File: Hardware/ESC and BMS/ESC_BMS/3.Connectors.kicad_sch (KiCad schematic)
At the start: 11 parts, among them J401 1mm2_connector, J402 1mm2_connector, J403 1mm2_connector, J404 JST_8PH_2mm, J405 JST_3PH_2mm, J406 1mm2_connector, J407 1mm2_connector, J408 1mm2_connector, J409 1mm2_connector, J410 DC power jack, J411 DC power jack GND

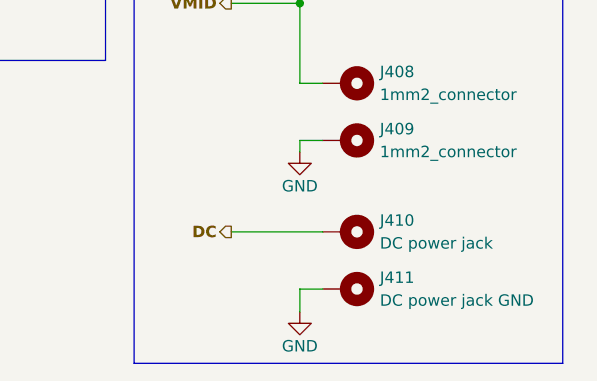
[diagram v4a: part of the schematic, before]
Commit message: ESC/BMS fully ready for PCB
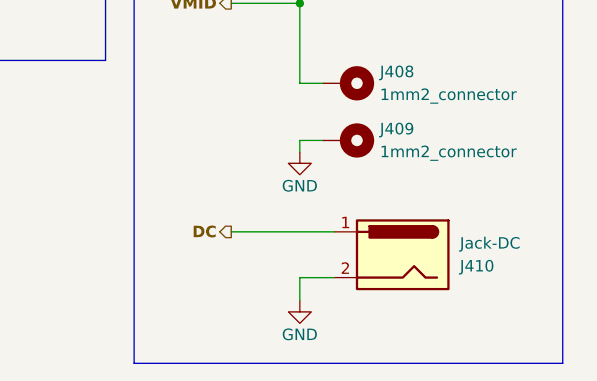
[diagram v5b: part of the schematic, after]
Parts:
- removed J410: DC power jack, Connector_Wire:SolderWire-1sqmm_1x01_D1.4mm_OD2.7mm, symbol Mechanical:MountingHole_Pad
- removed J411: DC power jack GND, Connector_Wire:SolderWire-1sqmm_1x01_D1.4mm_OD2.7mm, symbol Mechanical:MountingHole_Pad
- added J410: Jack-DC, Connector_BarrelJack:BarrelJack_Horizontal, symbol Connector:Jack-DC
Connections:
- net DC: now also J410.1
- net GND: now also J410.2
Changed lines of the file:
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@@
 	(wire
 		(pts
-			(xy 161.29 71.12) (xy 163.83 71.12)
+			(xy 161.29 69.85) (xy 165.1 69.85)
 		)
 		(stroke
@@
 	(wire
 		(pts
-			(xy 153.67 64.77) (xy 163.83 64.77)
+			(xy 153.67 64.77) (xy 165.1 64.77)
 		)
 		(stroke
@@
 	(wire
 		(pts
-			(xy 161.29 71.12) (xy 161.29 73.66)
+			(xy 161.29 69.85) (xy 161.29 72.39)
 		)
 		(stroke
@@
 			)
 			(justify right)
-		)
-	)
-	(symbol
-		(lib_id "Mechanical:MountingHole_Pad")
-		(at 166.37 71.12 270)
-		(unit 1)
-		(exclude_from_sim no)
-		(in_bom no)
-		(on_board yes)
-		(dnp no)
-		(fields_autoplaced yes)
-		(property "Reference" "J411"
-			(at 170.18 69.8499 90)
-			(effects
-				(font
-					(size 1.27 1.27)
-				)
-				(justify left)
-			)
-		)
-		(property "Value" "DC power jack GND"
-			(at 170.18 72.3899 90)
-			(effects
-				(font
-					(size 1.27 1.27)
-				)
-				(justify left)
-			)
-		)
-		(property "Footprint" "Connector_Wire:SolderWire-1sqmm_1x01_D1.4mm_OD2.7mm"
-			(at 166.37 71.12 0)
-			(effects
-				(font
-					(size 1.27 1.27)
-				)
-				(hide yes)
-			)
-		)
-		(property "Datasheet" "~"
-			(at 166.37 71.12 0)
-			(effects
-				(font
-					(size 1.27 1.27)
-				)
-				(hide yes)
-			)
-		)
-		(property "Description" "Mounting Hole with connection"
-			(at 166.37 71.12 0)
-			(effects
-				(font
-					(size 1.27 1.27)
-				)
-				(hide yes)
-			)
-		)
-		(pin "1"
-		)
-		(instances
-			(project "SPROJ3EE_ESC_BMS"
-				(path "/64aee9f2-a448-43ef-b28d-f00e276bd9f5/b843d17e-7d6d-4569-97d7-0fdd5bf8acb0"
-					(reference "J411")
-					(unit 1)
-				)
-			)
 		)
 	)
@@
 	)
 	(symbol
-		(lib_id "Mechanical:MountingHole_Pad")
-		(at 166.37 64.77 270)
-		(unit 1)
-		(exclude_from_sim no)
-		(in_bom no)
-		(on_board yes)
-		(dnp no)
-		(fields_autoplaced yes)
-		(property "Reference" "J410"
-			(at 170.18 63.4999 90)
-			(effects
-				(font
-					(size 1.27 1.27)
-				)
-				(justify left)
-			)
-		)
-		(property "Value" "DC power jack"
-			(at 170.18 66.0399 90)
-			(effects
-				(font
-					(size 1.27 1.27)
-				)
-				(justify left)
-			)
-		)
-		(property "Footprint" "Connector_Wire:SolderWire-1sqmm_1x01_D1.4mm_OD2.7mm"
-			(at 166.37 64.77 0)
-			(effects
-				(font
-					(size 1.27 1.27)
-				)
-				(hide yes)
-			)
-		)
-		(property "Datasheet" "~"
-			(at 166.37 64.77 0)
-			(effects
-				(font
-					(size 1.27 1.27)
-				)
-				(hide yes)
-			)
-		)
-		(property "Description" "Mounting Hole with connection"
-			(at 166.37 64.77 0)
-			(effects
-				(font
-					(size 1.27 1.27)
-				)
-				(hide yes)
-			)
-		)
-		(pin "1"
-		)
-		(instances
-			(project "SPROJ3EE_ESC_BMS"
-				(path "/64aee9f2-a448-43ef-b28d-f00e276bd9f5/b843d17e-7d6d-4569-97d7-0fdd5bf8acb0"
-					(reference "J410")
-					(unit 1)
-				)
-			)
-		)
-	)
-	(symbol
 		(lib_id "power:GND")
-		(at 161.29 73.66 0)
+		(at 161.29 72.39 0)
 		(unit 1)
 		(exclude_from_sim no)
@@
 		(dnp no)
 		(property "Reference" "#PWR0405"
-			(at 161.29 80.01 0)
+			(at 161.29 78.74 0)
 			(effects
 				(font
@@
 		)
 		(property "Value" "GND"
-			(at 161.29 77.47 0)
+			(at 161.29 76.2 0)
 			(effects
 				(font
@@
 		)
 		(property "Footprint" ""
-			(at 161.29 73.66 0)
+			(at 161.29 72.39 0)
 			(effects
 				(font
@@
 		)
 		(property "Datasheet" ""
-			(at 161.29 73.66 0)
+			(at 161.29 72.39 0)
 			(effects
 				(font
@@
 		)
 		(property "Description" "Power symbol creates a global label with name \"GND\" , ground"
-			(at 161.29 73.66 0)
+			(at 161.29 72.39 0)
 			(effects
 				(font
@@
 					(unit 1)
 				)
+			)
+		)
+	)
+	(symbol
+		(lib_id "Connector:Jack-DC")
+		(at 172.72 67.31 0)
+		(mirror y)
+		(unit 1)
+		(exclude_from_sim no)
+		(in_bom yes)
+		(on_board yes)
+		(dnp no)
+		(property "Reference" "J410"
+			(at 179.07 68.5801 0)
+			(effects
+				(font
+					(size 1.27 1.27)
+				)
+				(justify right)
+			)
+		)
+		(property "Value" "Jack-DC"
+			(at 179.07 66.0401 0)
+			(effects
+				(font
+					(size 1.27 1.27)
+				)
+				(justify right)
+			)
+		)
+		(property "Footprint" "Connector_BarrelJack:BarrelJack_Horizontal"
+			(at 171.45 68.326 0)
+			(effects
+				(font
+					(size 1.27 1.27)
+				)
+				(hide yes)
+			)
+		)
+		(property "Datasheet" "~"
+			(at 171.45 68.326 0)
+			(effects
+				(font
+					(size 1.27 1.27)
+				)
+				(hide yes)
+			)
+		)
+		(property "Description" "DC Barrel Jack"
+			(at 172.72 67.31 0)
+			(effects
+				(font
+					(size 1.27 1.27)
+				)
+				(hide yes)
+			)
+		)
+		(pin "2"
+		)
+		(pin "1"
+		)
+		(instances
+			(project ""
+				(path "/64aee9f2-a448-43ef-b28d-f00e276bd9f5/b843d17e-7d6d-4569-97d7-0fdd5bf8acb0"
+					(reference "J410")
+					(unit 1)
+				)

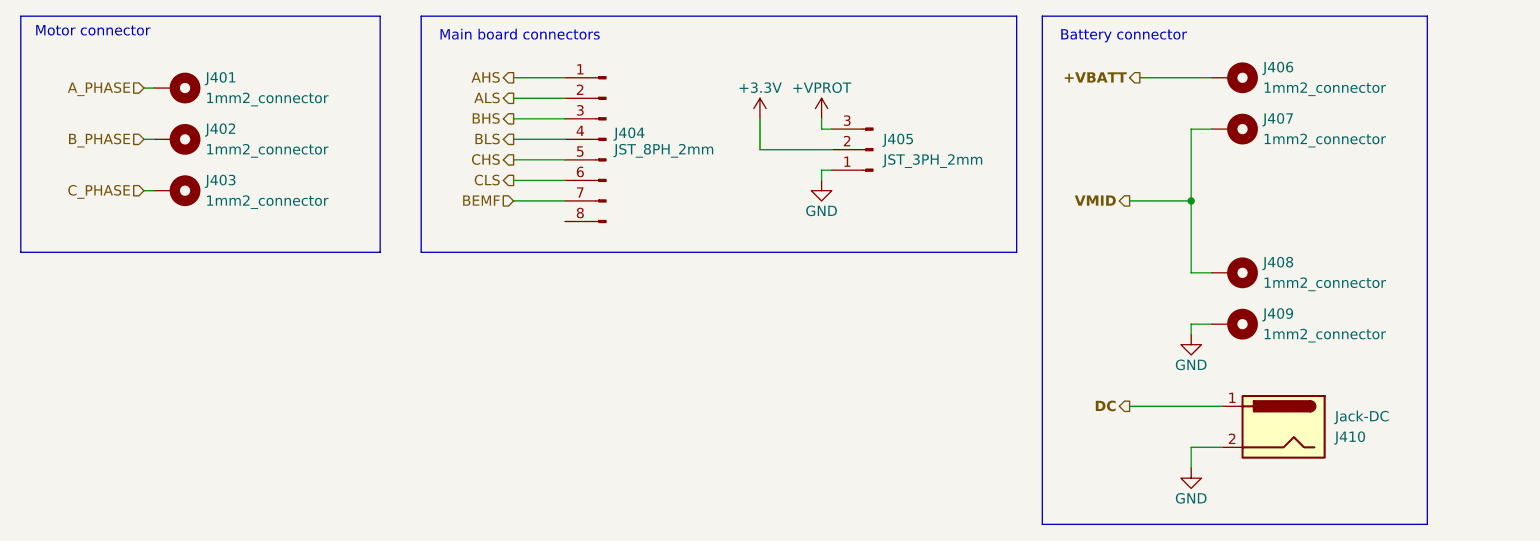
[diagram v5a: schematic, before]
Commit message: ESC/BMS PCB started
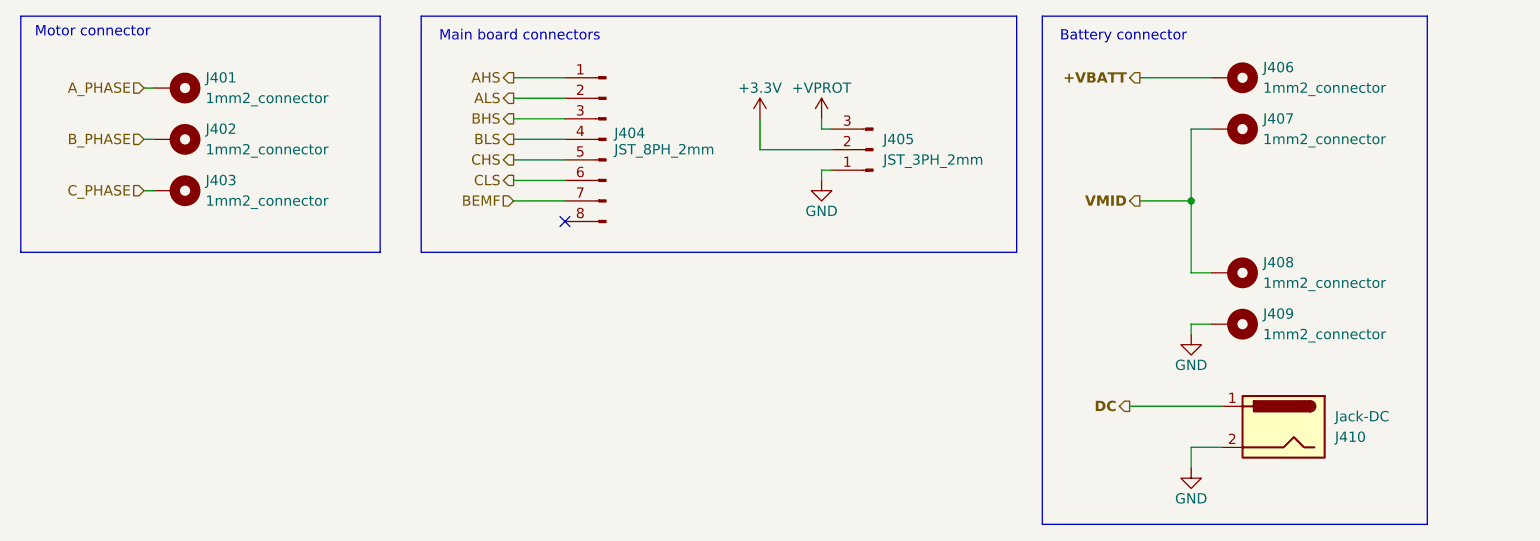
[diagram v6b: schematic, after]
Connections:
- no-connect marks 0 -> 1
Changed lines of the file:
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@@
 		(color 0 0 0 0)
 	)
+	(no_connect
+		(at 83.82 41.91)
+	)
 	(wire
 		(pts
@@
 	(wire
 		(pts
-			(xy 153.67 39.37) (xy 161.29 39.37)
+			(xy 154.94 39.37) (xy 161.29 39.37)
 		)
 		(stroke
@@
 	(hierarchical_label "VMID"
 		(shape output)
-		(at 153.67 39.37 180)
-		(effects
-			(font
+		(at 154.94 39.37 180)
+		(effects
+			(font

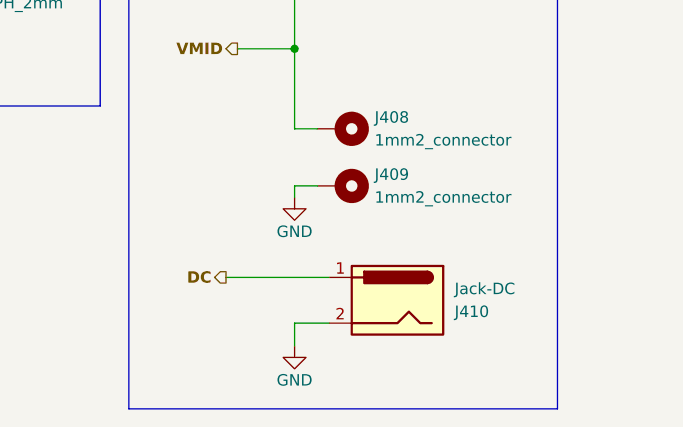
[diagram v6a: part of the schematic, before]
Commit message: ESC BMS component placement close to done
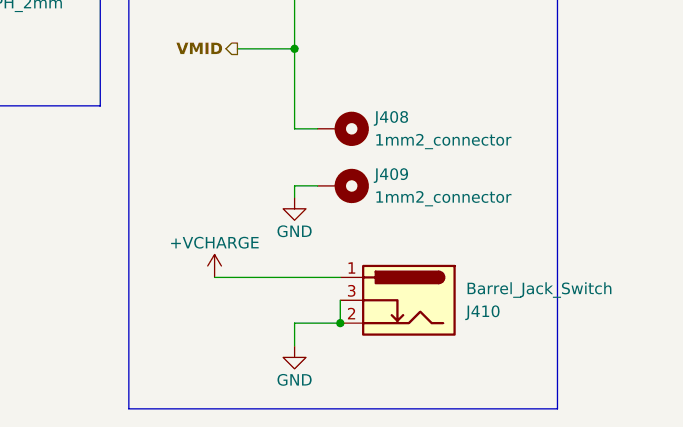
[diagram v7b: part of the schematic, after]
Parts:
- removed J410: Jack-DC, Connector_BarrelJack:BarrelJack_Horizontal, symbol Connector:Jack-DC
- added J410: Barrel_Jack_Switch, Connector_BarrelJack:BarrelJack_Horizontal, symbol Connector:Barrel_Jack_Switch
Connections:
- net GND: now also J410.2, J410.3
- new net +VCHARGE: J410.1
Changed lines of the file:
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@@
+		(color 0 0 0 0)
+	)
+	(junction
+		(at 166.37 69.85)
+		(diameter 0)
 		(color 0 0 0 0)
 	)
@@
 	(wire
 		(pts
+			(xy 152.4 64.77) (xy 166.37 64.77)
+		)
+		(stroke
+			(width 0)
+			(type default)
+		)
+	)
+	(wire
+		(pts
 			(xy 83.82 34.29) (xy 77.47 34.29)
 		)
@@
 	(wire
 		(pts
-			(xy 161.29 69.85) (xy 165.1 69.85)
+			(xy 161.29 69.85) (xy 166.37 69.85)
 		)
 		(stroke
@@
 	(wire
 		(pts
-			(xy 153.67 64.77) (xy 165.1 64.77)
-		)
-		(stroke
-			(width 0)
-			(type default)
-		)
-	)
-	(wire
-		(pts
 			(xy 83.82 31.75) (xy 77.47 31.75)
 		)
@@
 		(pts
 			(xy 115.57 35.56) (xy 115.57 36.83)
+		)
+		(stroke
+			(width 0)
+			(type default)
+		)
+	)
+	(wire
+		(pts
+			(xy 166.37 67.31) (xy 166.37 69.85)
 		)
 		(stroke
@@
 		)
 	)
-	(hierarchical_label "DC"
-		(shape output)
-		(at 153.67 64.77 180)
-		(effects
-			(font
-				(size 1.27 1.27)
-				(thickness 0.254)
-				(bold yes)
-			)
-			(justify right)
-		)
-	)
 	(hierarchical_label "BHS"
 		(shape output)
@@
 	)
 	(symbol
+		(lib_id "power:VBUS")
+		(at 152.4 64.77 0)
+		(unit 1)
+		(exclude_from_sim no)
+		(in_bom yes)
+		(on_board yes)
+		(dnp no)
+		(property "Reference" "#PWR0406"
+			(at 152.4 68.58 0)
+			(effects
+				(font
+					(size 1.27 1.27)
+				)
+				(hide yes)
+			)
+		)
+		(property "Value" "+VCHARGE"
+			(at 152.4 60.96 0)
+			(effects
+				(font
+					(size 1.27 1.27)
+				)
+			)
+		)
+		(property "Footprint" ""
+			(at 152.4 64.77 0)
+			(effects
+				(font
+					(size 1.27 1.27)
+				)
+				(hide yes)
+			)
+		)
+		(property "Datasheet" ""
+			(at 152.4 64.77 0)
+			(effects
+				(font
+					(size 1.27 1.27)
+				)
+				(hide yes)
+			)
+		)
+		(property "Description" "Power symbol creates a global label with name \"VBUS\""
+			(at 152.4 64.77 0)
+			(effects
+				(font
+					(size 1.27 1.27)
+				)
+				(hide yes)
+			)
+		)
+		(pin "1"
+		)
+		(instances
+			(project "SPROJ3EE_ESC_BMS"
+				(path "/64aee9f2-a448-43ef-b28d-f00e276bd9f5/b843d17e-7d6d-4569-97d7-0fdd5bf8acb0"
+					(reference "#PWR0406")
+					(unit 1)
+				)
+			)
+		)
+	)
+	(symbol
 		(lib_id "Connector:Conn_01x03_Pin")
 		(at 121.92 33.02 180)
@@
 	)
 	(symbol
-		(lib_id "Connector:Jack-DC")
-		(at 172.72 67.31 0)
-		(mirror y)
-		(unit 1)
-		(exclude_from_sim no)
-		(in_bom yes)
-		(on_board yes)
-		(dnp no)
-		(property "Reference" "J410"
-			(at 179.07 68.5801 0)
-			(effects
-				(font
-					(size 1.27 1.27)
-				)
-				(justify right)
-			)
-		)
-		(property "Value" "Jack-DC"
-			(at 179.07 66.0401 0)
-			(effects
-				(font
-					(size 1.27 1.27)
-				)
-				(justify right)
-			)
-		)
-		(property "Footprint" "Connector_BarrelJack:BarrelJack_Horizontal"
-			(at 171.45 68.326 0)
-			(effects
-				(font
-					(size 1.27 1.27)
-				)
-				(hide yes)
-			)
-		)
-		(property "Datasheet" "~"
-			(at 171.45 68.326 0)
-			(effects
-				(font
-					(size 1.27 1.27)
-				)
-				(hide yes)
-			)
-		)
-		(property "Description" "DC Barrel Jack"
-			(at 172.72 67.31 0)
-			(effects
-				(font
-					(size 1.27 1.27)
-				)
-				(hide yes)
-			)
-		)
-		(pin "2"
-		)
-		(pin "1"
-		)
-		(instances
-			(project ""
-				(path "/64aee9f2-a448-43ef-b28d-f00e276bd9f5/b843d17e-7d6d-4569-97d7-0fdd5bf8acb0"
-					(reference "J410")
-					(unit 1)
-				)
-			)
-		)
-	)
-	(symbol
 		(lib_id "Mechanical:MountingHole_Pad")
 		(at 35.56 38.1 270)
@@
 					(unit 1)
 				)
+			)
+		)
+	)
+	(symbol
+		(lib_id "Connector:Barrel_Jack_Switch")
+		(at 173.99 67.31 0)
+		(mirror y)
+		(unit 1)
+		(exclude_from_sim no)
+		(in_bom yes)
+		(on_board yes)
+		(dnp no)
+		(property "Reference" "J410"
+			(at 180.34 68.5801 0)
+			(effects
+				(font
+					(size 1.27 1.27)
+				)
+				(justify right)
+			)
+		)
+		(property "Value" "Barrel_Jack_Switch"
+			(at 180.34 66.0401 0)
+			(effects
+				(font
+					(size 1.27 1.27)
+				)
+				(justify right)
+			)
+		)
+		(property "Footprint" "Connector_BarrelJack:BarrelJack_Horizontal"
+			(at 172.72 68.326 0)
+			(effects
+				(font
+					(size 1.27 1.27)
+				)
+				(hide yes)
+			)
+		)
+		(property "Datasheet" "~"
+			(at 172.72 68.326 0)
+			(effects
+				(font
+					(size 1.27 1.27)
+				)
+				(hide yes)
+			)
+		)
+		(property "Description" "DC Barrel Jack with an internal switch"
+			(at 173.99 67.31 0)
+			(effects
+				(font
+					(size 1.27 1.27)
+				)
+				(hide yes)
+			)
+		)
+		(pin "3"
+		)
+		(pin "2"
+		)
+		(pin "1"
+		)
+		(instances
+			(project ""
+				(path "/64aee9f2-a448-43ef-b28d-f00e276bd9f5/b843d17e-7d6d-4569-97d7-0fdd5bf8acb0"
+					(reference "J410")
+					(unit 1)
+				)

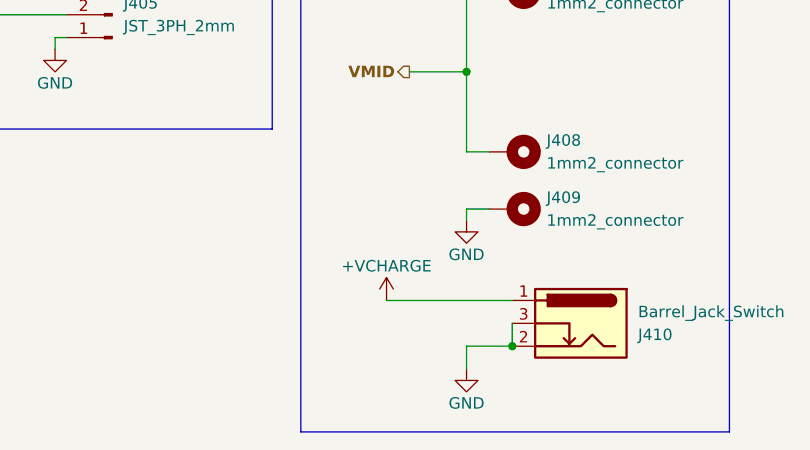
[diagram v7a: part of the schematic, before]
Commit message: ESC done
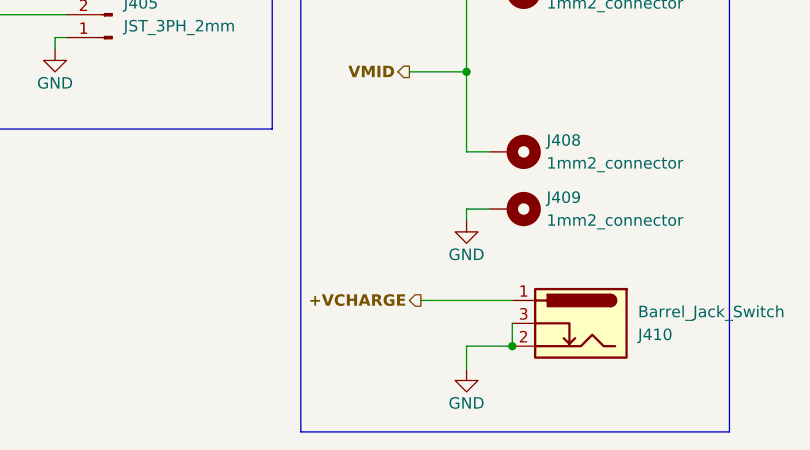
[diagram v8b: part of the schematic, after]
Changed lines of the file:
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@@
 	(wire
 		(pts
-			(xy 152.4 64.77) (xy 166.37 64.77)
+			(xy 156.21 64.77) (xy 166.37 64.77)
 		)
 		(stroke
@@
 		(shape output)
 		(at 154.94 39.37 180)
+		(effects
+			(font
+				(size 1.27 1.27)
+				(thickness 0.254)
+				(bold yes)
+			)
+			(justify right)
+		)
+	)
+	(hierarchical_label "+VCHARGE"
+		(shape output)
+		(at 156.21 64.77 180)
 		(effects
 			(font
@@
 					(unit 1)
 				)
-			)
-		)
-	)
-	(symbol
-		(lib_id "power:VBUS")
-		(at 152.4 64.77 0)
-		(unit 1)
-		(exclude_from_sim no)
-		(in_bom yes)
-		(on_board yes)
-		(dnp no)
-		(property "Reference" "#PWR0406"
-			(at 152.4 68.58 0)
-			(effects
-				(font
-					(size 1.27 1.27)
-				)
-				(hide yes)
-			)
-		)
-		(property "Value" "+VCHARGE"
-			(at 152.4 60.96 0)
-			(effects
-				(font
-					(size 1.27 1.27)
-				)
-			)
-		)
-		(property "Footprint" ""
-			(at 152.4 64.77 0)
-			(effects
-				(font
-					(size 1.27 1.27)
-				)
-				(hide yes)
-			)
-		)
-		(property "Datasheet" ""
-			(at 152.4 64.77 0)
-			(effects
-				(font
-					(size 1.27 1.27)
-				)
-				(hide yes)
-			)
-		)
-		(property "Description" "Power symbol creates a global label with name \"VBUS\""
-			(at 152.4 64.77 0)
-			(effects
-				(font
-					(size 1.27 1.27)
-				)
-				(hide yes)
-			)
-		)
-		(pin "1"
-		)
-		(instances
-			(project "SPROJ3EE_ESC_BMS"
-				(path "/64aee9f2-a448-43ef-b28d-f00e276bd9f5/b843d17e-7d6d-4569-97d7-0fdd5bf8acb0"
-					(reference "#PWR0406")
-					(unit 1)
-				)
